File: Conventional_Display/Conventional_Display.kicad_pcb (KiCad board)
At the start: 2 copper layers, 93 parts, among them J1 Conn_01x05_Female, U1 7-Segment_Display_CA, U10 7-Segment_Display_CA, U11 7-Segment_Display_CA, U12 7-Segment_Display_CA, U13 7-Segment_Display_CA, U14 7-Segment_Display_CA, U15 7-Segment_Display_CA, U16 MAX_7219, U17 MAX_7219, U18 MAX_7219, U19 MAX_7219, U2 7-Segment_Display_CA, U20 1088A5_8x8_LED_Matrix, U21 1088A5_8x8_LED_Matrix, U22 1088A5_8x8_LED_Matrix, U23 1088A5_8x8_LED_Matrix, U3 7-Segment_Display_CA, U4 7-Segment_Display_CA, U5 7-Segment_Display_CA, U6 7-Segment_Display_CA, U7 7-Segment_Display_CA, U8 7-Segment_Display_CA, U9 7-Segment_Display_CA

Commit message: Changes
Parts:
- added J2: Conn_01x03, Socket_Strips:Socket_Strip_Straight_1x03_Pitch2.54mm, B.Cu at (-2.54, 73.7)
- added REF**: 4_40_Hole, MRDT_Drill_Holes:4_40_Hole_Corner, F.Cu at (145.1, 124.8)
- added REF**: 4_40_Hole, MRDT_Drill_Holes:4_40_Hole_Corner, F.Cu at (68.5, 124.8)
- added REF**: 4_40_Hole, MRDT_Drill_Holes:4_40_Hole_Corner, F.Cu at (68.5, 49.2)
- added REF**: 4_40_Hole, MRDT_Drill_Holes:4_40_Hole_Corner, F.Cu at (145.1, 49.2)
- J1: value Conn_01x05_Female -> Conn_01x02; footprint MRDT_Connectors:MOLEX_SL_5_Horizontal -> Socket_Strips:Socket_Strip_Straight_1x02_Pitch2.54mm; moved to B.Cu
- moved J1 166.9 mm to (-13.5, 33.8)
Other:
- board outline added: 92.7 x 91.7 mm

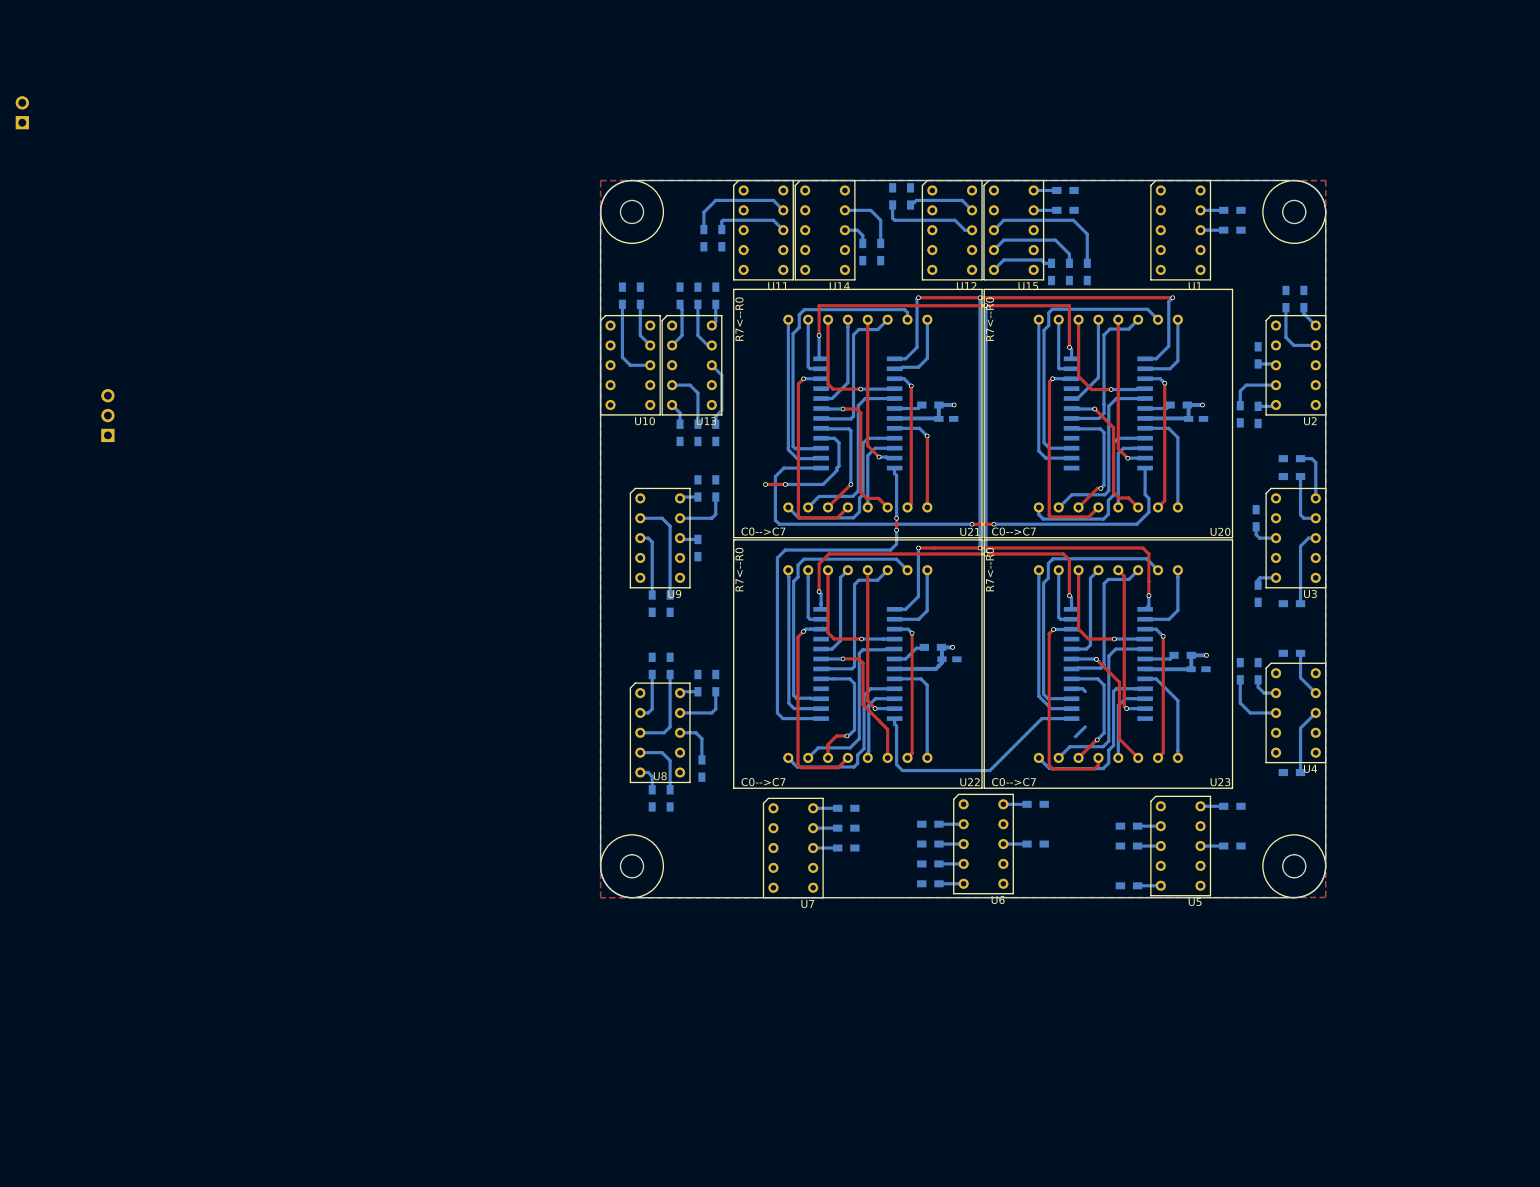
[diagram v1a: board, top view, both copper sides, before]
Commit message: Made Clock Board
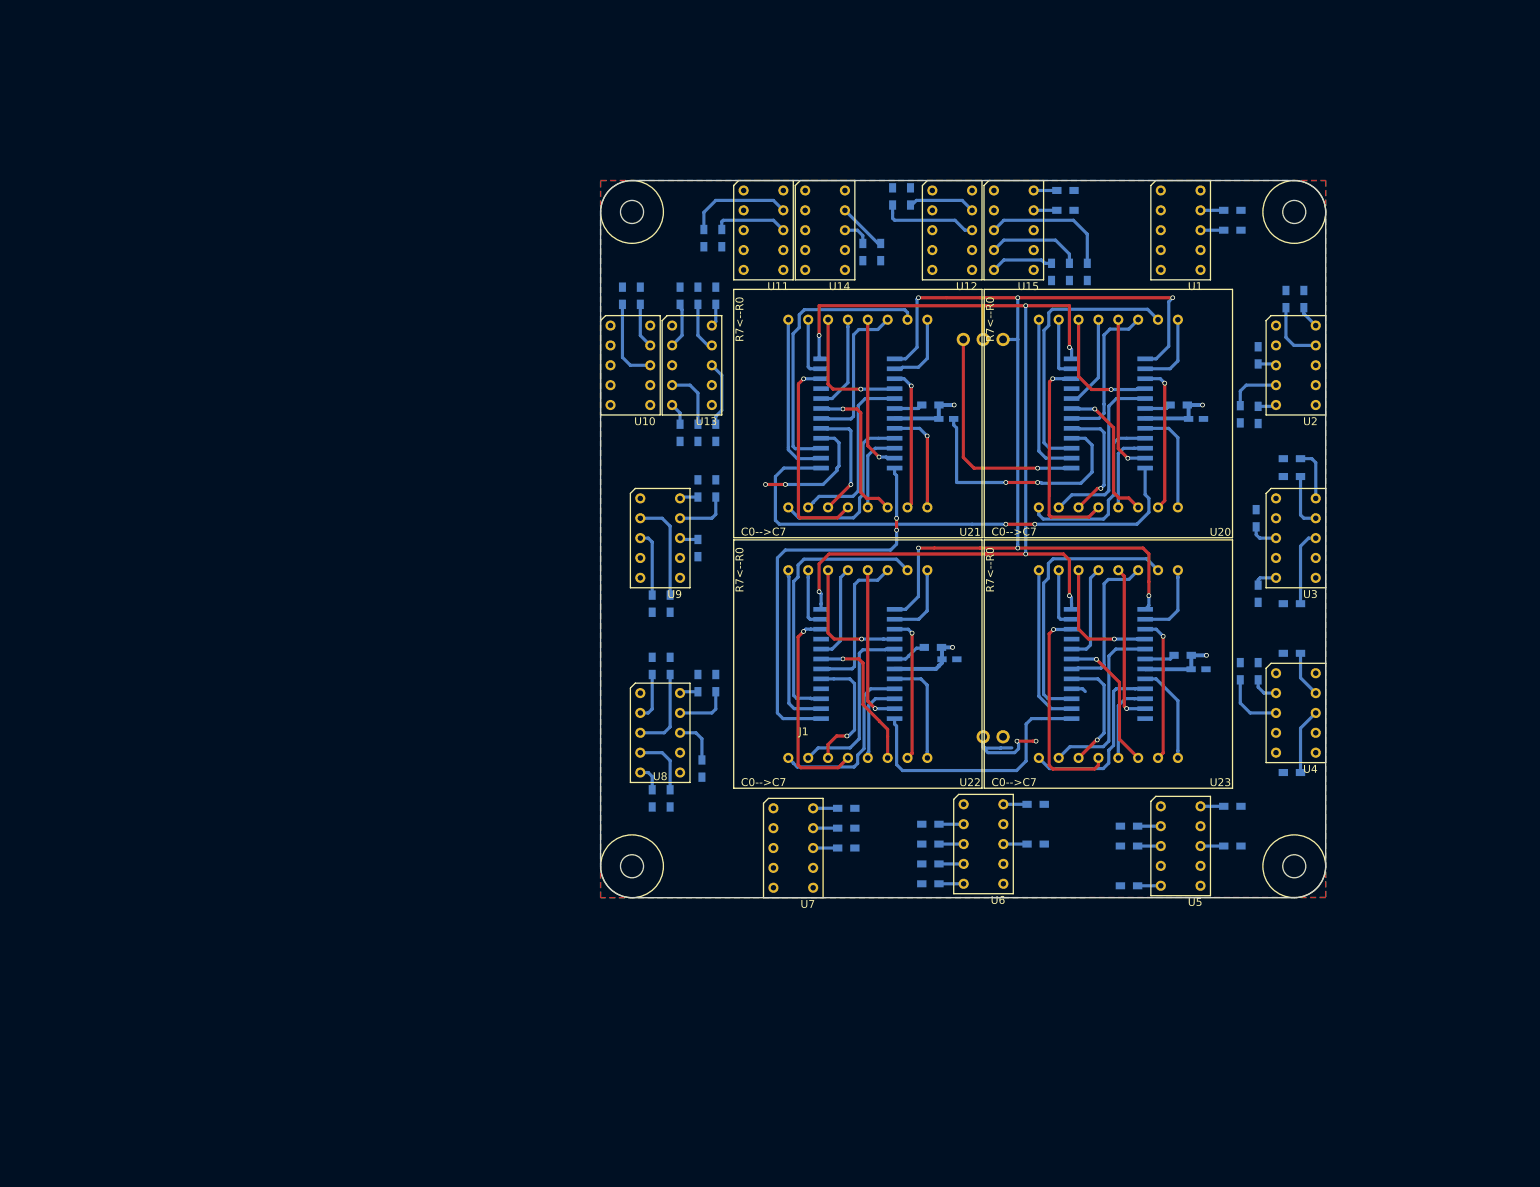
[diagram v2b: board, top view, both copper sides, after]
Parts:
- removed J2: Conn_01x03, Socket_Strips:Socket_Strip_Straight_1x03_Pitch2.54mm
- J1: value Conn_01x02 -> Conn_01x05; footprint Socket_Strips:Socket_Strip_Straight_1x02_Pitch2.54mm -> Project_Library:Clock_Board; moved to F.Cu
- moved J1 127.7 mm to (85.2, 114.8)
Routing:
- net GND: track 18.0 -> 65.4 mm, vias 2 -> 6
- net Din: track 0.00 -> 29.5 mm, vias 0 -> 1
- net Load: track 122.7 -> 127.1 mm
- net Net-(U18-Pad24): track 31.4 -> 34.2 mm
- net Clk: track 131.5 -> 133.4 mm
- net (no net): track 1.80 -> 0.00 mm
- net Net-(R55-Pad1): track 8.06 -> 6.33 mm

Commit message: generated Gerbs
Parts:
- moved R22 0.51 mm to (116.1, 121.4)
- moved R23 0.51 mm to (116.1, 126.5)
- moved R24 0.51 mm to (102.6, 131.6)
- moved R25 0.51 mm to (102.6, 129.0)
- moved R27 0.51 mm to (102.6, 126.5)
- moved U6 0.51 mm to (105.6, 132.8)
- moved R26 0.51 mm to (102.6, 124.0)
- moved U5 0.25 mm to (130.8, 132.8)
- moved R17 0.25 mm to (141.2, 121.4)
- moved R18 0.25 mm to (141.2, 126.5)
- moved R20 0.25 mm to (128.0, 124.0)
- moved R21 0.25 mm to (128.0, 126.5)
- moved R19 0.25 mm to (128.0, 131.6)
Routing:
- net GND: track 65.4 -> 34.2 mm, vias 6 -> 4
- net Net-(U17-Pad16): track 17.0 -> 16.2 mm

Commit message: Added silkscreen to boards and organized gerbs
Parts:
- added G***: LOGO, MRDT_Silkscreens:z_sig_Andrew_Van_Horn_Sig_15mm, F.Cu at (85.1, 76.6)
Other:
- board text added: "Conventional Display,Rev 1 Andrew Van Horn"

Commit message: re routed conventional display LED matrix traces.
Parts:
- moved C3 25.5 mm to (79.6, 101.6), turned to 180 degrees
- moved C4 25.4 mm to (111.6, 101.6), turned to 180 degrees
- moved C2 25.2 mm to (79.6, 69.6), turned to 180 degrees
- moved C1 25.1 mm to (111.6, 69.6), turned to 180 degrees
- moved R64 21.5 mm to (81.6, 103.4), turned to 0 degrees
- moved R65 21.3 mm to (113.6, 103.4), turned to 0 degrees
- moved R63 21.1 mm to (81.6, 71.4), turned to 0 degrees
- moved R62 20.8 mm to (113.6, 71.4), turned to 0 degrees
- moved U19 1.44 mm to (124.0, 102.7), turned to 180 degrees
- moved U16 1.44 mm to (124.0, 70.7), turned to 180 degrees
- moved U18 1.41 mm to (91.9, 102.7), turned to 180 degrees
- moved U17 1.41 mm to (91.9, 70.7), turned to 180 degrees
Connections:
- U1 pad 10: (no net) -> Net-(U1-Pad10)
- U1 pad 2: (no net) -> Net-(U1-Pad2)
- U1 pad 3: (no net) -> Net-(U1-Pad3)
- U1 pad 4: (no net) -> Net-(U1-Pad4)
- U1 pad 5: (no net) -> Net-(U1-Pad5)
- U1 pad 7: (no net) -> Net-(U1-Pad7)
- U10 pad 10: (no net) -> Net-(U10-Pad10)
- U10 pad 2: (no net) -> Net-(U10-Pad2)
- U10 pad 3: (no net) -> Net-(U10-Pad3)
- U10 pad 4: (no net) -> Net-(U10-Pad4)
- U10 pad 5: (no net) -> Net-(U10-Pad5)
- U10 pad 7: (no net) -> Net-(U10-Pad7)
- U11 pad 10: (no net) -> Net-(U11-Pad10)
- U11 pad 2: (no net) -> Net-(U11-Pad2)
- U11 pad 3: (no net) -> Net-(U11-Pad3)
- U11 pad 4: (no net) -> Net-(U11-Pad4)
- U11 pad 5: (no net) -> Net-(U11-Pad5)
- U11 pad 7: (no net) -> Net-(U11-Pad7)
- U12 pad 10: (no net) -> Net-(U12-Pad10)
- U12 pad 2: (no net) -> Net-(U12-Pad2)
- U12 pad 3: (no net) -> Net-(U12-Pad3)
- U12 pad 4: (no net) -> Net-(U12-Pad4)
- U12 pad 5: (no net) -> Net-(U12-Pad5)
- U12 pad 7: (no net) -> Net-(U12-Pad7)
- U13 pad 3: (no net) -> Net-(U13-Pad3)
- U13 pad 7: (no net) -> Net-(U13-Pad7)
- U14 pad 10: (no net) -> Net-(U14-Pad10)
- U14 pad 2: (no net) -> Net-(U14-Pad2)
- U14 pad 3: (no net) -> Net-(U14-Pad3)
- U14 pad 4: (no net) -> Net-(U14-Pad4)
- U14 pad 5: (no net) -> Net-(U14-Pad5)
- U14 pad 7: (no net) -> Net-(U14-Pad7)
- U15 pad 2: (no net) -> Net-(U15-Pad2)
- U15 pad 7: (no net) -> Net-(U15-Pad7)
- U15 pad 8: (no net) -> Net-(U15-Pad8)
- U19 pad 24: (no net) -> Net-(U19-Pad24)
- U2 pad 2: (no net) -> Net-(U2-Pad2)
- U2 pad 7: (no net) -> Net-(U2-Pad7)
- U2 pad 8: (no net) -> Net-(U2-Pad8)
- U20 pad 1: Net-(U16-Pad20) -> Net-(U16-Pad2)
- U20 pad 10: Net-(U16-Pad3) -> Net-(U16-Pad5)
- U20 pad 11: Net-(U16-Pad6) -> Net-(U16-Pad14)
- U20 pad 12: Net-(U16-Pad23) -> Net-(U16-Pad16)
- U20 pad 14: Net-(U16-Pad16) -> Net-(U16-Pad23)
- U20 pad 15: Net-(U16-Pad11) -> Net-(U16-Pad10)
- U20 pad 16: Net-(U16-Pad2) -> Net-(U16-Pad6)
- U20 pad 2: Net-(U16-Pad15) -> Net-(U16-Pad20)
- U20 pad 3: Net-(U16-Pad7) -> Net-(U16-Pad21)
- U20 pad 4: Net-(U16-Pad22) -> Net-(U16-Pad7)
- U20 pad 5: Net-(U16-Pad10) -> Net-(U16-Pad22)
- U20 pad 6: Net-(U16-Pad5) -> Net-(U16-Pad11)
- U20 pad 7: Net-(U16-Pad17) -> Net-(U16-Pad15)
- U20 pad 8: Net-(U16-Pad21) -> Net-(U16-Pad17)
- U20 pad 9: Net-(U16-Pad14) -> Net-(U16-Pad3)
- U21 pad 1: Net-(U17-Pad20) -> Net-(U17-Pad2)
- U21 pad 10: Net-(U17-Pad3) -> Net-(U17-Pad5)
- U21 pad 11: Net-(U17-Pad6) -> Net-(U17-Pad14)
- U21 pad 12: Net-(U17-Pad23) -> Net-(U17-Pad16)
- U21 pad 14: Net-(U17-Pad16) -> Net-(U17-Pad23)
- U21 pad 15: Net-(U17-Pad11) -> Net-(U17-Pad10)
- U21 pad 16: Net-(U17-Pad2) -> Net-(U17-Pad6)
- U21 pad 2: Net-(U17-Pad15) -> Net-(U17-Pad20)
- U21 pad 3: Net-(U17-Pad7) -> Net-(U17-Pad21)
- U21 pad 4: Net-(U17-Pad22) -> Net-(U17-Pad7)
- U21 pad 5: Net-(U17-Pad10) -> Net-(U17-Pad22)
- U21 pad 6: Net-(U17-Pad5) -> Net-(U17-Pad11)
- U21 pad 7: Net-(U17-Pad17) -> Net-(U17-Pad15)
- U21 pad 8: Net-(U17-Pad21) -> Net-(U17-Pad17)
- U21 pad 9: Net-(U17-Pad14) -> Net-(U17-Pad3)
- U22 pad 1: Net-(U18-Pad20) -> Net-(U18-Pad2)
- U22 pad 10: Net-(U18-Pad3) -> Net-(U18-Pad5)
- U22 pad 11: Net-(U18-Pad6) -> Net-(U18-Pad14)
- U22 pad 12: Net-(U18-Pad23) -> Net-(U18-Pad16)
- U22 pad 14: Net-(U18-Pad16) -> Net-(U18-Pad23)
- U22 pad 15: Net-(U18-Pad11) -> Net-(U18-Pad10)
- U22 pad 16: Net-(U18-Pad2) -> Net-(U18-Pad6)
- U22 pad 2: Net-(U18-Pad15) -> Net-(U18-Pad20)
- U22 pad 3: Net-(U18-Pad7) -> Net-(U18-Pad21)
- U22 pad 4: Net-(U18-Pad22) -> Net-(U18-Pad7)
- U22 pad 5: Net-(U18-Pad10) -> Net-(U18-Pad22)
- U22 pad 6: Net-(U18-Pad5) -> Net-(U18-Pad11)
- U22 pad 7: Net-(U18-Pad17) -> Net-(U18-Pad15)
- U22 pad 8: Net-(U18-Pad21) -> Net-(U18-Pad17)
- U22 pad 9: Net-(U18-Pad14) -> Net-(U18-Pad3)
- U23 pad 1: Net-(U19-Pad20) -> Net-(U19-Pad2)
- U23 pad 10: Net-(U19-Pad3) -> Net-(U19-Pad5)
- U23 pad 11: Net-(U19-Pad6) -> Net-(U19-Pad14)
- U23 pad 12: Net-(U19-Pad23) -> Net-(U19-Pad16)
- U23 pad 14: Net-(U19-Pad16) -> Net-(U19-Pad23)
- U23 pad 15: Net-(U19-Pad11) -> Net-(U19-Pad10)
- U23 pad 16: Net-(U19-Pad2) -> Net-(U19-Pad6)
- U23 pad 2: Net-(U19-Pad15) -> Net-(U19-Pad20)
- U23 pad 3: Net-(U19-Pad7) -> Net-(U19-Pad21)
- U23 pad 4: Net-(U19-Pad22) -> Net-(U19-Pad7)
- U23 pad 5: Net-(U19-Pad10) -> Net-(U19-Pad22)
- U23 pad 6: Net-(U19-Pad5) -> Net-(U19-Pad11)
- U23 pad 7: Net-(U19-Pad17) -> Net-(U19-Pad15)
- U23 pad 8: Net-(U19-Pad21) -> Net-(U19-Pad17)
- U23 pad 9: Net-(U19-Pad14) -> Net-(U19-Pad3)
- U3 pad 2: (no net) -> Net-(U3-Pad2)
- U3 pad 4: (no net) -> Net-(U3-Pad4)
- U3 pad 7: (no net) -> Net-(U3-Pad7)
- U4 pad 10: (no net) -> Net-(U4-Pad10)
- U4 pad 4: (no net) -> Net-(U4-Pad4)
- U4 pad 5: (no net) -> Net-(U4-Pad5)
- U4 pad 7: (no net) -> Net-(U4-Pad7)
- U5 pad 4: (no net) -> Net-(U5-Pad4)
- U5 pad 7: (no net) -> Net-(U5-Pad7)
- U5 pad 9: (no net) -> Net-(U5-Pad9)
- U6 pad 7: (no net) -> Net-(U6-Pad7)
- U6 pad 9: (no net) -> Net-(U6-Pad9)
- U7 pad 2: (no net) -> Net-(U7-Pad2)
- U7 pad 3: (no net) -> Net-(U7-Pad3)
- U7 pad 4: (no net) -> Net-(U7-Pad4)
- U7 pad 5: (no net) -> Net-(U7-Pad5)
- U7 pad 7: (no net) -> Net-(U7-Pad7)
- U8 pad 7: (no net) -> Net-(U8-Pad7)
- U9 pad 4: (no net) -> Net-(U9-Pad4)
- U9 pad 5: (no net) -> Net-(U9-Pad5)
- U9 pad 7: (no net) -> Net-(U9-Pad7)
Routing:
- net +5V: track 38.2 -> 84.6 mm, vias 4 -> 11
- net Net-(U16-Pad24): track 66.3 -> 24.0 mm, vias 2 -> 0
- net GND: track 34.2 -> 5.33 mm, vias 4 -> 30
- net Net-(U18-Pad24): track 34.6 -> 62.8 mm, vias 0 -> 2
- net Load: track 127.1 -> 150.3 mm, vias 6 -> 2
- net Net-(U19-Pad11): track 7.78 -> 27.8 mm, vias 0 -> 1
- net Net-(U18-Pad11): track 7.78 -> 27.8 mm, vias 0 -> 1
- net Net-(U17-Pad11): track 7.78 -> 27.8 mm, vias 0 -> 1
- net Net-(U16-Pad11): track 7.87 -> 27.8 mm, vias 0 -> 1
- net Net-(U19-Pad10): track 27.5 -> 10.4 mm, vias 1 -> 0
- net Net-(U17-Pad10): track 27.1 -> 10.4 mm, vias 1 -> 0
- net Net-(U16-Pad10): track 27.0 -> 10.4 mm, vias 1 -> 0
- net Net-(U18-Pad10): track 26.8 -> 10.4 mm, vias 1 -> 0
- net Net-(U17-Pad23): track 20.2 -> 32.5 mm
- net Net-(U19-Pad23): track 20.5 -> 32.5 mm
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- added copper zone on F.Cu, net GND
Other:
- board text added: "Conventional Display, Rev 2 Andrew Van Horn"
- board text removed: "Conventional Display,Rev 1 Andrew Van Horn"
